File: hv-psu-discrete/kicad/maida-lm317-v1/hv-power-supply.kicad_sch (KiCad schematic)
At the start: 90 parts, among them J1 AC-LV, J10 GND_LV, J11 AC-HV, J12 AC-HV, J13 EARTH, J2 AC-LV, J3 HV, J4 GND_HV, J5 LV, J6 GND_LV, J7 LED, J8 GND_LV, J9 +5V, K1 G6S-2 DC5, Q1 LND150N3-G, Q2 IRF840, Q3 MMBT3904, U1 LT3080xST, U2 LM317_TO-220, U3 LM7805_TO220, U4 TLC555xD

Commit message: WIP
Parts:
- removed C12: 1uF/630V, Capacitor_THT:C_Rect_L26.5mm_W10.5mm_P22.50mm_MKS4, symbol Device:C
- removed C13: 2.2uF, Capacitor_THT:CP_Radial_D5.0mm_P2.50mm, symbol Device:C_Polarized
- removed C23: 2.2uF/630V, Capacitor_THT:C_Rect_L33.0mm_W15.0mm_P27.50mm_MKS4, symbol Device:C
- removed C7: 100nF/630V, Capacitor_THT:C_Rect_L18.0mm_W5.0mm_P15.00mm_FKS3_FKP3, symbol Device:C
- removed D10, D9: MMSZ5237C/8.2V, Diode_SMD:D_SOD-123, symbol Diode:1N47xxA
- removed D15, D17: 1N4007, Diode_SMD:D_SMA_Handsoldering, symbol Diode:1N4007
- removed D16: MMSZ20T1G/20V, Diode_SMD:D_SOD-123, symbol Diode:1N47xxA
- removed Q1: LND150N3-G, Package_TO_SOT_SMD:SOT-89-3, symbol Device:Q_NMOS_SGD
- removed Q2: IRF840, Package_TO_SOT_THT:TO-220-3_Vertical, symbol Transistor_FET:IRF740
- removed U1: LT3080xST, Package_TO_SOT_SMD:SOT-223, symbol Regulator_Linear:LT3080xST
- added C7, C8: 1uF/400V, Capacitor_THT:CP_Radial_D6.3mm_P2.50mm, symbol Device:C_Polarized
- added C9: 100nF/630V, Capacitor_THT:C_Rect_L18.0mm_W5.0mm_P15.00mm_FKS3_FKP3, symbol Device:C
- added D10: P6KE530A, Diode_THT:D_DO-15_P12.70mm_Horizontal, symbol Diode:1.5KExxA
- added D15, D9: 1N5245B/0.5W, Diode_THT:D_DO-35_SOD27_P7.62mm_Horizontal, symbol Diode:1N53xxB
- added D16: 1N4148, Diode_THT:D_DO-35_SOD27_P7.62mm_Horizontal, symbol Diode:1N4148
- added D17: P6KE39A, Diode_THT:D_DO-15_P12.70mm_Horizontal, symbol Diode:1.5KExxA
- added HS4: Heatsink, Heatsink:Heatsink_Fischer_SK129-STS_42x25mm_2xDrill2.5mm, symbol Mechanical:Heatsink
- added Q1: FQPF2N70, Package_TO_SOT_THT:TO-220-3_Vertical, symbol Transistor_FET:IRF740
- added R23: 2.7R/1W, Resistor_THT:R_Axial_DIN0207_L6.3mm_D2.5mm_P10.16mm_Horizontal, symbol Device:R
- added R24: 100R/2W, Resistor_THT:R_Axial_DIN0414_L11.9mm_D4.5mm_P15.24mm_Horizontal, symbol Device:R
- added R25: 300k/0.6W, Resistor_THT:R_Axial_DIN0207_L6.3mm_D2.5mm_P10.16mm_Horizontal, symbol Device:R
- added R26: 100k/0.6W, Resistor_THT:R_Axial_DIN0207_L6.3mm_D2.5mm_P10.16mm_Horizontal, symbol Device:R
- added U1: LM317_TO-220, Package_TO_SOT_THT:TO-220-3_Vertical, symbol Regulator_Linear:LM317_TO-220
- R2: value 4.7k -> 200k/2W; footprint Resistor_SMD:R_0805_2012Metric_Pad1.20x1.40mm_HandSolder -> Resistor_THT:R_Axial_DIN0414_L11.9mm_D4.5mm_P15.24mm_Horizontal
- R21: value 100k/2W -> 18k/3W; footprint Resistor_THT:R_Axial_DIN0414_L11.9mm_D4.5mm_P15.24mm_Horizontal -> Resistor_THT:R_Axial_DIN0614_L14.3mm_D5.7mm_P20.32mm_Horizontal
- R22: value 100k/2W -> 121R/0.6W; footprint Resistor_THT:R_Axial_DIN0414_L11.9mm_D4.5mm_P15.24mm_Horizontal -> Resistor_THT:R_Axial_DIN0207_L6.3mm_D2.5mm_P10.16mm_Horizontal
- R3: value 100R -> 100k/2W; footprint Resistor_SMD:R_0805_2012Metric_Pad1.20x1.40mm_HandSolder -> Resistor_THT:R_Axial_DIN0414_L11.9mm_D4.5mm_P15.24mm_Horizontal
- R4: value 20R/0.6W -> 1k/0.6W
- R5: value 100k/0.6W -> 100R/2W; footprint Resistor_THT:R_Axial_DIN0207_L6.3mm_D2.5mm_P10.16mm_Horizontal -> Resistor_THT:R_Axial_DIN0414_L11.9mm_D4.5mm_P15.24mm_Horizontal
- R6: value 1k/0.6W -> 121R/0.6W
- RV1: value 500k -> 2k
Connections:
- net GND_HV: now also R2.2, C7.2, C8.2, C9.1, R26.2; no longer R21.2, R22.2
- net GND_LV: now also R24.1
- net at R21.1, R22.1, R6.2: now also U1.1 (ADJ); no longer D18.1 (K), J3.1 (Pin_1)
- net at C10.1, C11.1, D14.1 (K)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: now also R2.1, R3.1, D10.1 (A1), Q1.2 (D)
- net at R3.2: now also R4.2, D15.1 (K), D9.1 (K)
- net at R4.1: now also Q1.1 (G)
- net at R5.2: now also D17.1 (A1), U1.3 (VI)
- new net: D16.1 (K), D17.2 (A2), D18.1 (K), D9.2 (A), J3.1 (Pin_1), R22.2, R23.1, R25.1, U1.2 (VO)
- new net: R21.2, RV1.1
- new net: D10.2 (A2), D15.2 (A), Q1.3 (S), R5.1
- new net: C7.1, D16.2 (A), R6.1
- new net: C8.1, R23.2
- new net: C9.2, R24.2, R25.2, R26.1
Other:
- note removed: "D9/D10 => voltage greater dropout U1 + Q2 gate source voltage"
- title: HV Power Supply -> HV Power Supply LM317 Maida
- moved on the sheet: D18, HS1

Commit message: Wip
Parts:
- HS4: footprint Heatsink:Heatsink_Fischer_SK129-STS_42x25mm_2xDrill2.5mm -> Heatsink:Heatsink_Fischer_SK104-STC-STIC_35x13mm_2xDrill2.5mm
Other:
- note added: "Vout=1.25*(1+(RV1+R21)/R22) R21 power rating > Vout*Vout/R21 Current values: 187V..207V"
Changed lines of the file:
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@@
     (stroke (width 0) (type default) (color 0 0 0 0))
+  )
+  (text "13,4°/W" (at 294.64 35.56 0)
+    (effects (font (size 1.27 1.27)) (justify left bottom))
   )
   (text "Snubber" (at 39.37 209.55 0)
     (effects (font (size 1.27 1.27)) (justify left bottom))
   )
-  (text "3.7°/W" (at 293.37 35.56 0)
-    (effects (font (size 1.27 1.27)) (justify left bottom))
-  )
   (text "Cs=100nF/630V\nRs=470R/0.6W" (at 57.15 83.82 0)
     (effects (font (size 1.27 1.27)) (justify left bottom))
@@
   )
   (text "3.7°/W" (at 227.33 35.56 0)
+    (effects (font (size 1.27 1.27)) (justify left bottom))
+  )
+  (text "Vout=1.25*(1+(RV1+R21)/R22)\nR21 power rating > Vout*Vout/R21\nCurrent values: 187V..207V"
+    (at 329.565 24.765 0)
     (effects (font (size 1.27 1.27)) (justify left bottom))
   )
@@
     (pin "2")
   )
-  (symbol (lib_id "Mechanical:Heatsink") (at 289.56 33.02 0) (unit 1)
-    (in_bom yes) (on_board yes)
-    (property "Reference" "HS4" (id 0) (at 293.1668 29.9466 0)
-      (effects (font (size 1.27 1.27)) (justify left))
-    )
-    (property "Value" "Heatsink" (id 1) (at 293.1668 32.258 0)
-      (effects (font (size 1.27 1.27)) (justify left))
-    )
-    (property "Footprint" "Heatsink:Heatsink_Fischer_SK129-STS_42x25mm_2xDrill2.5mm" (id 2) (at 289.8648 33.02 0)
-      (effects (font (size 1.27 1.27)) hide)
-    )
-    (property "Datasheet" "~" (id 3) (at 289.8648 33.02 0)
-      (effects (font (size 1.27 1.27)) hide)
-    )
-  )
   (symbol (lib_id "Diode:1N4148") (at 252.73 77.47 90) (unit 1)
     (in_bom yes) (on_board yes) (fields_autoplaced)
@@
     (pin "1")
     (pin "2")
+  )
+  (symbol (lib_id "Mechanical:Heatsink") (at 290.83 33.02 0) (unit 1)
+    (in_bom yes) (on_board yes)
+    (property "Reference" "HS4" (id 0) (at 294.4368 29.9466 0)
+      (effects (font (size 1.27 1.27)) (justify left))
+    )
+    (property "Value" "Heatsink" (id 1) (at 294.4368 32.258 0)
+      (effects (font (size 1.27 1.27)) (justify left))
+    )
+    (property "Footprint" "Heatsink:Heatsink_Fischer_SK104-STC-STIC_35x13mm_2xDrill2.5mm" (id 2) (at 291.1348 33.02 0)
+      (effects (font (size 1.27 1.27)) hide)
+    )
+    (property "Datasheet" "~" (id 3) (at 291.1348 33.02 0)
+      (effects (font (size 1.27 1.27)) hide)
+    )
   )
   (symbol (lib_id "Diode:1.5KExxA") (at 223.52 42.545 0) (unit 1)
@@
       (reference "HS3") (unit 1) (value "Heatsink") (footprint "Heatsink:Heatsink_Fischer_SK129-STS_42x25mm_2xDrill2.5mm")
     )
-    (path "/571235b1-20be-45cf-8ba8-9f76b43c194b"
-      (reference "HS4") (unit 1) (value "Heatsink") (footprint "Heatsink:Heatsink_Fischer_SK129-STS_42x25mm_2xDrill2.5mm")
+    (path "/d8a97981-bc61-40d3-956f-aa9e3052900c"
+      (reference "HS4") (unit 1) (value "Heatsink") (footprint "Heatsink:Heatsink_Fischer_SK104-STC-STIC_35x13mm_2xDrill2.5mm")
     )
     (path "/00000000-0000-0000-0000-0000613ceb6b"

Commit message: Update hv-power-supply.kicad_sch
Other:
- note added: "Vin=27.3V -> Vout=22.1V Vin=340V, Vout=200V, Iidle=11mA Vin=340V, Vout=200V, Iload=50mA => THS1 after 10 minute stabilized to 73Grad"
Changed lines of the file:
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@@
   (title_block
     (title "HV Power Supply LM317 Maida")
-    (date "2022-08-19")
+    (date "2022-09-11")
     (rev "1")
   )
@@
     (effects (font (size 1.27 1.27)) (justify left bottom))
   )
+  (text "Vin=27.3V -> Vout=22.1V\nVin=340V, Vout=200V, Iidle=11mA\nVin=340V, Vout=200V, Iload=50mA => THS1 after 10 minute stabilized to 73Grad"
+    (at 37.465 142.24 0)
+    (effects (font (size 1.27 1.27)) (justify left bottom))
+  )

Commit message: WIP
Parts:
- D18: footprint Diode_SMD:D_SMA_Handsoldering -> Diode_THT:D_DO-41_SOD81_P10.16mm_Horizontal
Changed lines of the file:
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@@
     (title "HV Power Supply LM317 Maida")
     (date "2022-09-11")
-    (rev "1")
+    (rev "2")
   )
   (junction (at 213.36 138.43) (diameter 0) (color 0 0 0 0)
@@
     (property "Reference" "D18" (id 0) (at 347.7768 82.55 0))
     (property "Value" "1N4007" (id 1) (at 345.4654 82.55 0))
-    (property "Footprint" "Diode_SMD:D_SMA_Handsoldering" (id 2) (at 337.82 82.55 0)
+    (property "Footprint" "Diode_THT:D_DO-41_SOD81_P10.16mm_Horizontal" (id 2) (at 337.82 82.55 0)
       (effects (font (size 1.27 1.27)) hide)
     )
@@
     )
     (path "/00000000-0000-0000-0000-00006131394b"
-      (reference "D18") (unit 1) (value "1N4007") (footprint "Diode_SMD:D_SMA_Handsoldering")
+      (reference "D18") (unit 1) (value "1N4007") (footprint "Diode_THT:D_DO-41_SOD81_P10.16mm_Horizontal")
     )
     (path "/00000000-0000-0000-0000-00006017bc66"

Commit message: Update hv-power-supply.kicad_sch
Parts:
- D15, D9: value 1N5245B/0.5W -> 1N5245B/15V/0.5W
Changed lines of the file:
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@@
   (symbol (lib_id "Diode:1N53xxB") (at 237.49 62.865 90) (unit 1)
     (in_bom yes) (on_board yes) (fields_autoplaced)
-    (property "Reference" "D15" (id 0) (at 240.665 61.5949 90)
+    (property "Reference" "D15" (id 0) (at 240.03 61.5949 90)
       (effects (font (size 1.27 1.27)) (justify right))
     )
-    (property "Value" "1N5245B/0.5W" (id 1) (at 240.665 64.1349 90)
+    (property "Value" "1N5245B/15V/0.5W" (id 1) (at 240.03 64.1349 90)
       (effects (font (size 1.27 1.27)) (justify right))
     )
@@
       (effects (font (size 1.27 1.27)) (justify left))
     )
-    (property "Value" "1N5245B/0.5W" (id 1) (at 212.09 81.2799 90)
+    (property "Value" "1N5245B/15V/0.5W" (id 1) (at 212.09 81.2799 90)
       (effects (font (size 1.27 1.27)) (justify left))
     )
@@
     )
     (path "/e5c6a644-3134-4624-be7b-4b8179c64816"
-      (reference "D9") (unit 1) (value "1N5245B/0.5W") (footprint "Diode_THT:D_DO-35_SOD27_P7.62mm_Horizontal")
+      (reference "D9") (unit 1) (value "1N5245B/15V/0.5W") (footprint "Diode_THT:D_DO-35_SOD27_P7.62mm_Horizontal")
     )
     (path "/d915d000-e9a2-486b-a19d-b6ecd5d517c1"
@@
     )
     (path "/bb288774-3bbc-4c99-983e-2ab900dd5ab8"
-      (reference "D15") (unit 1) (value "1N5245B/0.5W") (footprint "Diode_THT:D_DO-35_SOD27_P7.62mm_Horizontal")
+      (reference "D15") (unit 1) (value "1N5245B/15V/0.5W") (footprint "Diode_THT:D_DO-35_SOD27_P7.62mm_Horizontal")
     )
     (path "/5e75c6c9-7e6b-47ff-b411-57cae7346819"

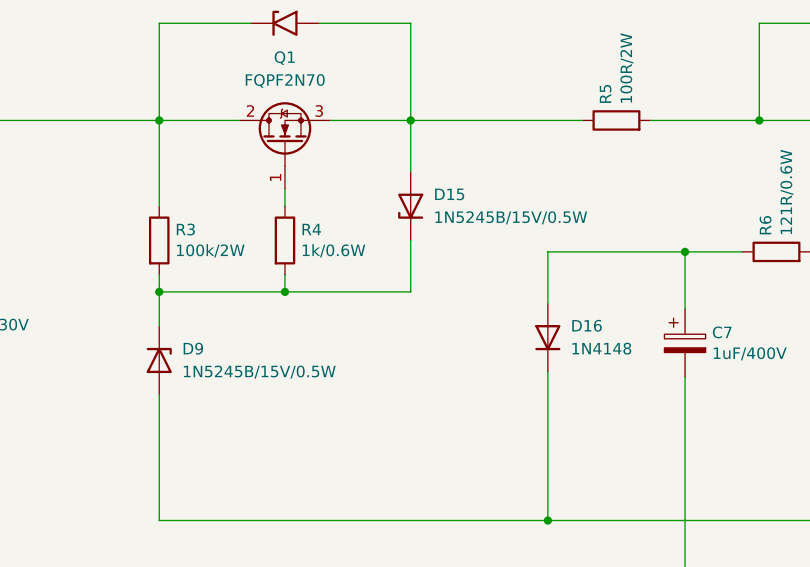
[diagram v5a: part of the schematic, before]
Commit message: Fix revision screw up
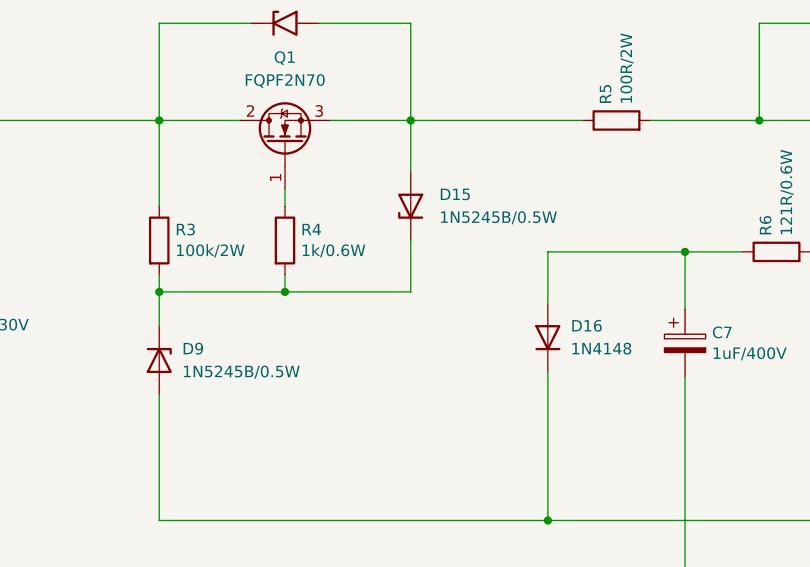
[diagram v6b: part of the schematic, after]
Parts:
- D15, D9: value 1N5245B/15V/0.5W -> 1N5245B/0.5W
- D18: footprint Diode_THT:D_DO-41_SOD81_P10.16mm_Horizontal -> Diode_SMD:D_SMA_Handsoldering
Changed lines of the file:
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@@
     (title "HV Power Supply LM317 Maida")
     (date "2022-09-11")
-    (rev "2")
+    (rev "1")
   )
   (junction (at 213.36 138.43) (diameter 0) (color 0 0 0 0)
@@
     (property "Reference" "D18" (id 0) (at 347.7768 82.55 0))
     (property "Value" "1N4007" (id 1) (at 345.4654 82.55 0))
-    (property "Footprint" "Diode_THT:D_DO-41_SOD81_P10.16mm_Horizontal" (id 2) (at 337.82 82.55 0)
+    (property "Footprint" "Diode_SMD:D_SMA_Handsoldering" (id 2) (at 337.82 82.55 0)
       (effects (font (size 1.27 1.27)) hide)
     )
@@
   (symbol (lib_id "Diode:1N53xxB") (at 237.49 62.865 90) (unit 1)
     (in_bom yes) (on_board yes) (fields_autoplaced)
-    (property "Reference" "D15" (id 0) (at 240.03 61.5949 90)
+    (property "Reference" "D15" (id 0) (at 240.665 61.5949 90)
       (effects (font (size 1.27 1.27)) (justify right))
     )
-    (property "Value" "1N5245B/15V/0.5W" (id 1) (at 240.03 64.1349 90)
+    (property "Value" "1N5245B/0.5W" (id 1) (at 240.665 64.1349 90)
       (effects (font (size 1.27 1.27)) (justify right))
     )
@@
       (effects (font (size 1.27 1.27)) (justify left))
     )
-    (property "Value" "1N5245B/15V/0.5W" (id 1) (at 212.09 81.2799 90)
+    (property "Value" "1N5245B/0.5W" (id 1) (at 212.09 81.2799 90)
       (effects (font (size 1.27 1.27)) (justify left))
     )
@@
     )
     (path "/e5c6a644-3134-4624-be7b-4b8179c64816"
-      (reference "D9") (unit 1) (value "1N5245B/15V/0.5W") (footprint "Diode_THT:D_DO-35_SOD27_P7.62mm_Horizontal")
+      (reference "D9") (unit 1) (value "1N5245B/0.5W") (footprint "Diode_THT:D_DO-35_SOD27_P7.62mm_Horizontal")
     )
     (path "/d915d000-e9a2-486b-a19d-b6ecd5d517c1"
@@
     )
     (path "/bb288774-3bbc-4c99-983e-2ab900dd5ab8"
-      (reference "D15") (unit 1) (value "1N5245B/15V/0.5W") (footprint "Diode_THT:D_DO-35_SOD27_P7.62mm_Horizontal")
+      (reference "D15") (unit 1) (value "1N5245B/0.5W") (footprint "Diode_THT:D_DO-35_SOD27_P7.62mm_Horizontal")
     )
     (path "/5e75c6c9-7e6b-47ff-b411-57cae7346819"
@@
     )
     (path "/00000000-0000-0000-0000-00006131394b"
-      (reference "D18") (unit 1) (value "1N4007") (footprint "Diode_THT:D_DO-41_SOD81_P10.16mm_Horizontal")
+      (reference "D18") (unit 1) (value "1N4007") (footprint "Diode_SMD:D_SMA_Handsoldering")
     )
     (path "/00000000-0000-0000-0000-00006017bc66"
